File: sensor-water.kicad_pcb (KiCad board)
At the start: 2 copper layers, 82 parts, among them IC1 STM8S003F3P-RESCUE-sensor-wat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, P1 CONN_01X04, P2 CONN_01X01, P3 CONN_01X04, P4 CONN_01X03, P5 CONN_01X01, P6 CONN_01X01, P7 CONN_01X01, P8 CONN_01X01, P9 CONN_01X01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

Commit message: initial README.md
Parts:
- removed U10, U11, U3, U5, U6, U7: -6V5, mylib:VCC
- C10, C12, C7, D10, D11, D12, D5, D6, D7, R15, R16, R17: moved to F.Cu
- moved U8 52.4 mm to (205.6, 55.4)
- moved C7 51.5 mm to (84.5, 54.9), turned to 270 degrees
- moved C10 47.2 mm to (90.7, 55.0), turned to 270 degrees
- moved D5 46.1 mm to (87.4, 57.4), turned to 270 degrees
- moved C12 44.3 mm to (97.0, 55.2), turned to 270 degrees
- moved D6 41.6 mm to (94.0, 57.2), turned to 270 degrees
- moved D7 36.6 mm to (100.3, 57.6), turned to 270 degrees
- moved R15 31.1 mm to (80.5, 62.0), turned to 180 degrees
- moved D10 19.9 mm to (61.6, 54.4), turned to 0 degrees
- moved R17 18.4 mm to (68.5, 55.4), turned to 270 degrees
- moved D12 18.3 mm to (66.2, 55.3), turned to 90 degrees
- moved D11 13.9 mm to (62.7, 59.6), turned to 270 degrees
- moved R16 13.3 mm to (60.0, 59.6), turned to 90 degrees
- moved R5 1.00 mm to (105.7, 58.9)
- moved R18 0.43 mm to (74.9, 62.1)
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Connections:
- C11 pad 1: Net-(C11-Pad1) -> -9VA
- C13 pad 1: Net-(C11-Pad1) -> -9VA
- C14 pad 1: Net-(C11-Pad1) -> -9VA
- C15 pad 1: Net-(C11-Pad1) -> -9VA
- C16 pad 1: Net-(C11-Pad1) -> -9VA
- C2 pad 2: Net-(C2-Pad2) -> +9VA
- C3 pad 1: Net-(C3-Pad1) -> -9VA
- C4 pad 2: Net-(C4-Pad2) -> +9VA
- C5 pad 2: Net-(C4-Pad2) -> +9VA
- C6 pad 2: Net-(C4-Pad2) -> +9VA
- C8 pad 2: Net-(C4-Pad2) -> +9VA
- C9 pad 2: Net-(C4-Pad2) -> +9VA
- P1 pad 4: Net-(P1-Pad4) -> +9VA
- U1 pad 4: Net-(U1-Pad4) -> -9VA
- U1 pad 8: Net-(U1-Pad8) -> +9VA
- U12 pad 1: Net-(U12-Pad1) -> +9VA
- U12 pad 3: Net-(U12-Pad1) -> +9VA
- U16 pad 11: Net-(U16-Pad11) -> +9VA
- U16 pad 4: Net-(U16-Pad11) -> +9VA
- U4 pad 5: Net-(C3-Pad1) -> -9VA
- U4 pad 8: Net-(C2-Pad2) -> +9VA
- U9 pad 4: Net-(U3-Pad1) -> -9VA
- U9 pad 8: Net-(U9-Pad8) -> +9VA

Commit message: initial kicad-sensor-water
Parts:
- D11, P4, Q1, Q2, R16, R23: moved to B.Cu
- moved R20 48.1 mm to (149.5, 59.8)
- moved R19 47.7 mm to (146.6, 59.7)
- moved R13 47.6 mm to (138.8, 54.8), turned to 270 degrees
- moved C17 47.5 mm to (144.1, 55.1), turned to 0 degrees
- moved D13 46.4 mm to (148.9, 55.1)
- moved U1 46.1 mm to (138.8, 59.5)
- moved D8 45.4 mm to (131.3, 59.6)
- moved D9 45.3 mm to (131.2, 61.8)
- moved R7 45.2 mm to (131.2, 57.4)
- moved R8 45.2 mm to (131.1, 55.0)
- moved Q1 41.4 mm to (191.1, 54.9)
- moved R10 38.9 mm to (186.2, 53.5)
- moved R9 38.9 mm to (185.9, 56.3)
- moved IC1 38.8 mm to (175.9, 57.9)
- moved C18 38.7 mm to (173.2, 56.0)
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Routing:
- net GND: track 0.00 -> 182.1 mm, vias 0 -> 6
- net /CON-OUT: track 0.00 -> 75.1 mm, vias 0 -> 1
- net Net-(R14-Pad1): track 0.00 -> 72.3 mm
- net Net-(R4-Pad1): track 0.00 -> 51.9 mm, vias 0 -> 2
- net /W-3: track 0.00 -> 39.2 mm, vias 0 -> 3
- net +9VA: track 0.00 -> 34.8 mm
- net /CON-IN: track 0.00 -> 32.7 mm, vias 0 -> 1
- net /WATER-E: track 0.00 -> 29.1 mm
- net Net-(D9-Pad1): track 0.00 -> 25.1 mm
- net VCC: track 0.00 -> 24.9 mm, vias 0 -> 1
- net Net-(R19-Pad2): track 0.00 -> 21.7 mm, vias 0 -> 2
- net Net-(R1-Pad2): track 0.00 -> 18.2 mm, vias 0 -> 2
- net -9VA: track 0.00 -> 18.1 mm
- net Net-(R2-Pad1): track 0.00 -> 17.9 mm
- net /COND: track 0.00 -> 14.7 mm
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
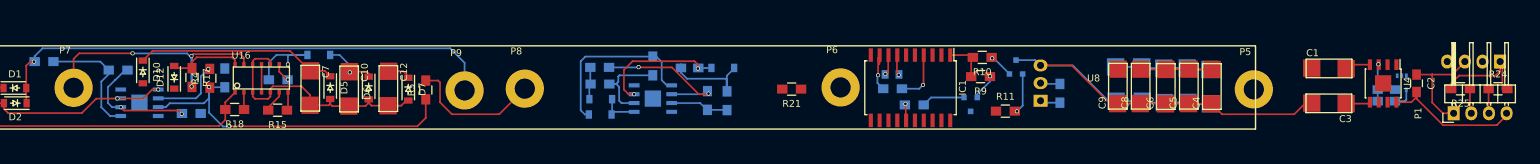
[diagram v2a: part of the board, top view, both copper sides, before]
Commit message: initial kicad-sensor-water
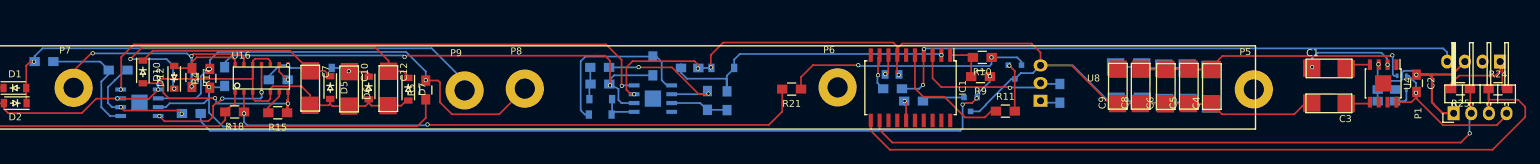
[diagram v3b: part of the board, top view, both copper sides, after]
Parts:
- moved D11 1.89 mm to (91.0, 55.1)
- moved Q1 0.75 mm to (190.9, 55.7), turned to 0 degrees
- moved R12 0.55 mm to (176.3, 59.8)
- moved P6 0.43 mm to (165.4, 57.8)
- moved R15 0.37 mm to (84.8, 61.5)
- moved R18 0.35 mm to (78.6, 61.4)
- moved R6 0.18 mm to (77.2, 56.3)
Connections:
- IC1 pad 13: /WATER-ON -> Net-(IC1-Pad13)
- IC1 pad 5: Net-(IC1-Pad5) -> /WATER-ON
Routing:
- net /COND-PWM: track 3.90 -> 121.3 mm, vias 1 -> 3
- net GND: track 182.1 -> 289.6 mm, vias 6 -> 9
- net /I2C_SDA: track 3.55 -> 111.0 mm
- net /I2C_SCL: track 3.69 -> 94.2 mm, vias 0 -> 1
- net -9VA: track 18.1 -> 102.1 mm, vias 0 -> 2
- net Net-(R18-Pad1): track 2.49 -> 85.7 mm, vias 0 -> 2
- net /NRST: track 7.32 -> 85.3 mm, vias 1 -> 2
- net Net-(R13-Pad2): track 14.1 -> 74.3 mm, vias 0 -> 2
- net +9VA: track 34.8 -> 86.9 mm, vias 0 -> 5
- net /WATER-L: track 3.34 -> 53.4 mm, vias 0 -> 2
- net /CON-IN: track 32.7 -> 67.9 mm, vias 1 -> 3
- net /WATER-PWM: track 3.59 -> 36.1 mm, vias 1 -> 2
- net /COND: track 14.7 -> 46.1 mm, vias 0 -> 1
- net Net-(D10-Pad2): track 2.64 -> 28.8 mm, vias 0 -> 2
- net /SENSOR: track 3.78 -> 23.5 mm, vias 0 -> 1
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
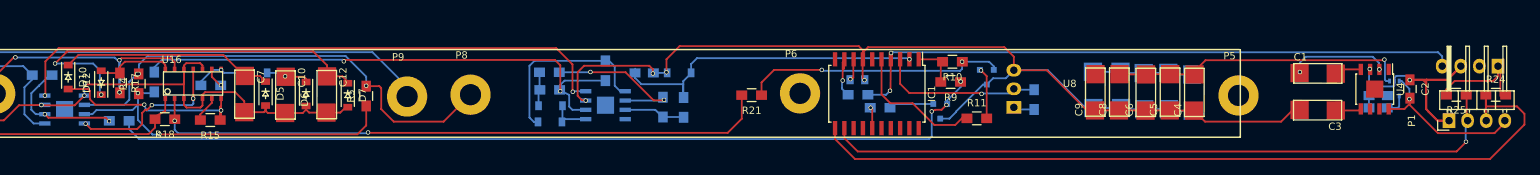
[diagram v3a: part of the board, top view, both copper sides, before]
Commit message: initial kicad-sensor-water
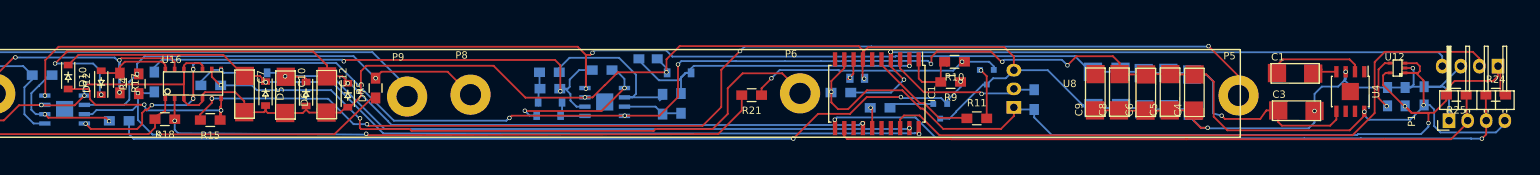
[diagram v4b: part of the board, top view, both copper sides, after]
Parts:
- C2: moved to B.Cu
- U12: moved to F.Cu
- moved C3 7.96 mm to (230.6, 60.3), turned to 0 degrees
- moved C20 3.68 mm to (248.0, 58.3), turned to 90 degrees
- moved U4 3.36 mm to (240.5, 57.6)
- moved C1 3.08 mm to (230.5, 55.2)
- moved U12 2.83 mm to (247.0, 54.4), turned to 90 degrees
- moved R22 2.36 mm to (171.0, 57.7)
- moved C2 2.15 mm to (250.6, 58.2)
- moved C19 2.00 mm to (245.6, 58.3), turned to 90 degrees
- moved C17 2.00 mm to (144.6, 53.1)
- moved R5 1.68 mm to (107.4, 57.1)
- moved D9 0.90 mm to (131.0, 60.9)
- moved R20 0.65 mm to (149.1, 59.2)
- moved D8 0.49 mm to (131.2, 59.1)
- moved R13 0.46 mm to (138.3, 54.7), turned to 180 degrees
- moved U1 0.45 mm to (138.7, 59.0)
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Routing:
- net +9VA: track 86.9 -> 241.1 mm, vias 5 -> 12
- net /W-1: track 3.24 -> 156.9 mm, vias 0 -> 4
- net VCC: track 24.9 -> 131.9 mm, vias 1 -> 3
- net -9VA: track 102.1 -> 202.5 mm, vias 2 -> 4
- net /WATER-E: track 29.1 -> 122.6 mm, vias 0 -> 2
- net /SWIM: track 0.00 -> 91.9 mm
- net /W-2: track 2.86 -> 92.7 mm, vias 1 -> 2
- net /WATER-N: track 6.14 -> 94.5 mm, vias 1 -> 2
- net /WATER-L: track 53.4 -> 127.0 mm, vias 2 -> 4
- net GND: track 289.6 -> 311.4 mm, vias 9 -> 10
- net /I2C_SDA: track 111.0 -> 97.1 mm, vias 0 -> 2
- net Net-(D9-Pad1): track 25.1 -> 20.3 mm, vias 0 -> 2
- net /CON-IN: track 67.9 -> 63.3 mm, vias 3 -> 2
- net Net-(C19-Pad1): track 3.15 -> 7.56 mm, vias 0 -> 1
- net /NRST: track 85.3 -> 89.5 mm, vias 2 -> 3
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
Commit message: initial kicad-sensor-water
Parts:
- moved U8 1.63 mm to (205.5, 57.0)
- moved R22 1.16 mm to (172.1, 57.7)
- moved P3 0.90 mm to (261.6, 54.1)
- moved R3 0.55 mm to (50.6, 54.2)
- moved P9 0.35 mm to (111.9, 57.9)
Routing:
- net /W-3: track 38.2 -> 33.1 mm
- net VCC: track 131.9 -> 135.5 mm
- net GND: track 311.4 -> 308.2 mm
- net Net-(R13-Pad2): track 74.0 -> 70.9 mm
- net /W-1: track 156.9 -> 155.1 mm
- net (no net): track 1.70 -> 0.00 mm
- net /W-2: track 92.7 -> 91.2 mm
- net Net-(R18-Pad1): track 85.2 -> 83.8 mm
- net Net-(R2-Pad1): track 17.9 -> 19.3 mm
- net /WATER-L: track 127.0 -> 125.7 mm
- net +9VA: track 241.1 -> 242.2 mm
- net /PWM1: track 9.53 -> 8.43 mm
- net -9VA: track 202.5 -> 201.5 mm
- net /NRST: track 89.5 -> 88.5 mm
- net /COND-PWM: track 120.5 -> 119.7 mm
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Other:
- net class Default: trace_width 0.25 -> 0.3; via_dia 0.6 -> 0.8

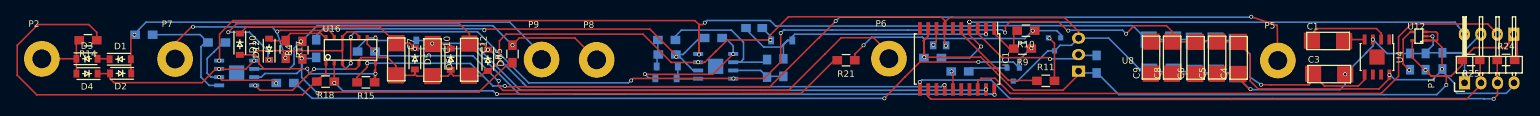
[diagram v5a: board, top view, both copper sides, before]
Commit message: initial kicad-sensor-water
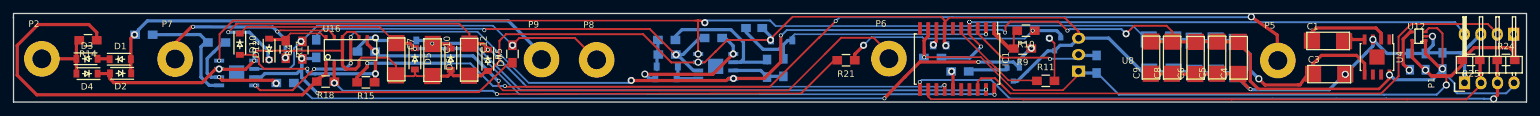
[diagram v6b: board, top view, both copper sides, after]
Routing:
- net VCC: track 135.5 -> 129.2 mm
- net +9VA: track 242.2 -> 245.6 mm
- net GND: track 308.2 -> 306.7 mm
- net -9VA: track 201.5 -> 203.0 mm
- net /W-1: track 155.1 -> 154.2 mm
- net /COND: track 45.6 -> 46.2 mm
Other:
- board outline added: 233 x 13.6 mm
- net class Default: clearance 0.2 -> 0.25; via_dia 0.8 -> 1.1; via_drill 0.4 -> 0.7
- rule trace_clearance: 0.2 -> 0.25
- rule trace_min: 0.2 -> 0.3
- rule via_min_size: 0.4 -> 0.6

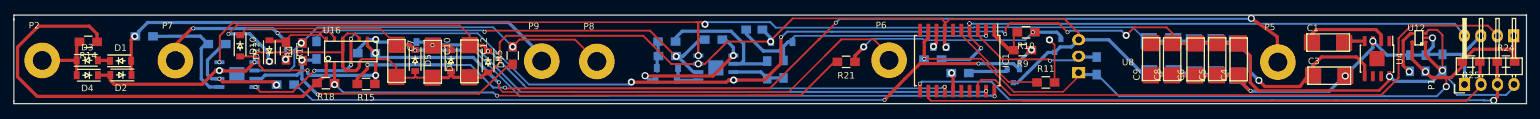
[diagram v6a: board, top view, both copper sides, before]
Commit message: initial kicad-sensor-water
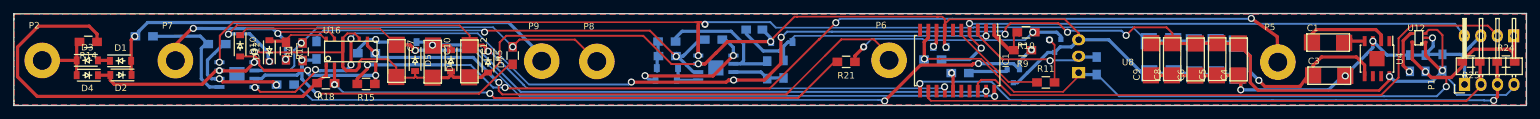
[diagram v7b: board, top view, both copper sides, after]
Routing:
- net GND: track 306.7 -> 307.7 mm
- net /W-2: track 91.2 -> 92.1 mm
- added copper zone on B.Cu, net GND
- added copper zone on F.Cu, net GND
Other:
- board size 233 x 13.6 mm -> 233.1 x 14.2 mm

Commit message: initial kicad-sensor-water
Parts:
- removed C11, C13: 100nF/50V, mylib:C_2920
- removed C18: 1u/50V, Capacitors_SMD:C_0805
- removed P4: CONN_01X03, Pin_Headers:Pin_Header_Angled_1x03
- removed U8: -6V5, mylib:VCC
- added R26: 10K, Resistors_SMD:R_0805_HandSoldering, F.Cu at (128.5, 42.8)
- added U2: DS18B20, TO_SOT_Packages_THT:TO-92_Horizontal2_Inline_Narrow_Oval, F.Cu at (245.6, 40.4)
- C1, C3: value 100nF/10V -> 100uF/16V; footprint mylib:C_2920 -> Capacitors_SMD:C_1206_HandSoldering
- C10, C12, C6, C7, C8, C9: footprint mylib:C_2920 -> Capacitors_SMD:C_0805_HandSoldering
- C14, C15, C16: footprint mylib:C_2920 -> Capacitors_SMD:C_0805_HandSoldering; moved to F.Cu
- C17, C19, C20, D11, D13, D8, D9, P3, Q1, Q2, R1, R12, R13, R16, R19, R2, R20, R22, R23, R3, R6, R7, R8: moved to F.Cu
- C2: value 10nF/10V -> 10uF/16V; footprint Capacitors_SMD:C_0805_HandSoldering -> Capacitors_SMD:C_1206_HandSoldering; moved to F.Cu
- C4, C5: value 100nF/50V -> 100nF/16V; footprint mylib:C_2920 -> Capacitors_SMD:C_0805_HandSoldering
- IC1: value STM8S003F3P-RESCUE-sensor-water -> STM32F030F4P6; footprint Housings_SOIC:SOIC-20_7.5x12.8mm_Pitch1.27mm -> mylib:STM32F030F4P6
- P1: moved to B.Cu
- U1, U9: footprint Housings_SOIC:SOIC-8-1EP_3.9x4.9mm_Pitch1.27mm -> Housings_SOIC:SOIC-8_3.9x4.9mm_Pitch1.27mm; moved to F.Cu
- U4: footprint Housings_SOIC:SOIC-8-1EP_3.9x4.9mm_Pitch1.27mm -> Housings_SOIC:SOIC-8_3.9x4.9mm_Pitch1.27mm
- moved P2 238.8 mm to (273.0, 39.4)
- moved P1 213.1 mm to (42.5, 35.4), turned to 180 degrees
- moved C2 202.9 mm to (48.2, 43.5), turned to 0 degrees
- moved P7 198.6 mm to (253.2, 39.3)
- moved U12 187.4 mm to (60.5, 36.5), turned to 270 degrees
- moved U4 185.2 mm to (56.0, 41.5), turned to 180 degrees
- moved C20 184.3 mm to (65.1, 35.8), turned to 0 degrees
- moved C3 183.6 mm to (48.2, 39.6)
- moved C19 181.6 mm to (65.2, 38.2), turned to 0 degrees
- moved P3 179.0 mm to (83.0, 42.3), turned to 180 degrees
- moved R14 170.8 mm to (211.5, 34.4)
- moved R17 168.7 mm to (239.9, 35.4), turned to 0 degrees
- moved C1 165.6 mm to (65.3, 42.1)
- moved D12 164.6 mm to (233.2, 35.3), turned to 180 degrees
- moved R15 156.5 mm to (239.9, 40.3)
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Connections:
- C14 pad 1: -9VA -> -12VA
- C15 pad 1: -9VA -> -12VA
- C16 pad 1: -9VA -> -12VA
- C2 pad 2: +9VA -> +12V
- C20 pad 1: VCC -> +3V3
- C3 pad 1: -9VA -> GND
- C3 pad 2: GND -> -12VA
- C4 pad 2: +9VA -> +3V3
- C5 pad 1: GND -> +3V3
- C5 pad 2: +9VA -> GND
- C6 pad 2: +9VA -> +12V
- C8 pad 2: +9VA -> +12V
- C9 pad 2: +9VA -> +12V
- IC1 pad 1: /PWM1 -> Net-(IC1-Pad1)
- IC1 pad 10: Net-(IC1-Pad10) -> /COND
- IC1 pad 11: /I2C_SDA -> Net-(IC1-Pad11)
- IC1 pad 12: /I2C_SCL -> /PWM1
- IC1 pad 14: /WATER-L -> Net-(IC1-Pad14)
- IC1 pad 15: /COND-OFF -> GND
- IC1 pad 16: Net-(IC1-Pad16) -> +3V3
- IC1 pad 17: Net-(IC1-Pad17) -> /COND-OFF
- IC1 pad 18: /SWIM -> /WATER-ON
- IC1 pad 19: /WATER-N -> /SWDIO
- IC1 pad 2: /COND -> /I2C_SDA
- IC1 pad 20: /WATER-E -> /SWCLK
- IC1 pad 3: /SENSOR -> /I2C_SCL
- IC1 pad 5: /WATER-ON -> +3V3
- IC1 pad 6: Net-(IC1-Pad6) -> /WATER-L
- IC1 pad 7: GND -> /WATER-N
- IC1 pad 8: Net-(C18-Pad1) -> /WATER-E
- IC1 pad 9: VCC -> /SENSOR
- P1 pad 4: +9VA -> +12V
- P3 pad 1: VCC -> +3V3
- P3 pad 2: /SWIM -> /SWDIO
- P3 pad 3: GND -> /SWCLK
- P3 pad 4: /NRST -> GND
- R22 pad 2: VCC -> +3V3
- R23 pad 2: VCC -> +3V3
- R24 pad 2: VCC -> +3V3
- R25 pad 2: VCC -> +3V3
- U1 pad 4: -9VA -> -12VA
- U1 pad 8: +9VA -> +12V
- U12 pad 1: +9VA -> +12V
- U12 pad 3: +9VA -> +12V
- U12 pad 5: VCC -> +3V3
- U16 pad 11: +9VA -> +12V
- U16 pad 4: +9VA -> +12V
- U4 pad 5: -9VA -> -12VA
- U4 pad 8: +9VA -> +12V
- U9 pad 4: -9VA -> -12VA
- U9 pad 8: +9VA -> +12V
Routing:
- net +9VA: track 246.0 -> 0.00 mm, vias 12 -> 0
- net -9VA: track 203.0 -> 0.00 mm, vias 4 -> 0
- net /WATER-OUT: track 10.7 -> 155.8 mm, vias 0 -> 2
- net VCC: track 129.2 -> 0.00 mm, vias 3 -> 0
- net /W-1: track 154.2 -> 25.6 mm, vias 4 -> 2
- net /WATER-L: track 125.7 -> 5.11 mm, vias 4 -> 0
- net Net-(R1-Pad2): track 18.2 -> 134.0 mm
- net +3V3: track 0.00 -> 110.7 mm, vias 0 -> 3
- net /WATER-E: track 122.3 -> 28.2 mm
- net /WATER-N: track 94.5 -> 2.32 mm, vias 2 -> 0
- net /SWIM: track 91.1 -> 0.00 mm
- net /COND-PWM: track 119.8 -> 29.8 mm
- net /NRST: track 88.5 -> 5.97 mm, vias 3 -> 0
- net Net-(R18-Pad1): track 84.3 -> 4.58 mm, vias 2 -> 0
- net +12V: track 0.00 -> 77.9 mm, vias 0 -> 3
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- removed copper zone on B.Cu, net GND
- removed copper zone on F.Cu, net GND
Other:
- board outline removed
- net class Default: clearance 0.25 -> 0.3
- rule pad_to_mask_clearance: 0.2 -> 0
- rule trace_clearance: 0.25 -> 0.3
- rule trace_min: 0.3 -> 0.2
- rule via_min_size: 0.6 -> 0.4
